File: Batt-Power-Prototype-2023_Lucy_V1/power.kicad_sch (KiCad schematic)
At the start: 62 parts, among them J1 Conn_01x02_Pin, U1 RPA60-2412SFW, U3 AZ1117IH-5.0, U5 AP62250Z6, U5 AZ1117-3.3

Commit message: added a bunch of footprints and other stuff...
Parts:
- CESH107M100AH4AA1: renamed from C1; footprint Capacitor_THT:CP_Radial_D8.0mm_P3.50mm -> Capacitor_THT:CP_Radial_D10.0mm_P5.00mm
- D2: footprint (none) -> Package_TO_SOT_SMD:TO-252-3_TabPin2
- renumbered C3 to needstobe2kv1, C4 to needstobe2kv2, C2 to needstobe50V1
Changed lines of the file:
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@@
   (junction (at 102.87 54.61) (diameter 0) (color 0 0 0 0)
   )
-  (junction (at 49.53 45.72) (diameter 0) (color 0 0 0 0)
-  )
   (junction (at 123.19 124.46) (diameter 0) (color 0 0 0 0)
   )
@@
   (junction (at 148.59 40.64) (diameter 0) (color 0 0 0 0)
   )
-  (junction (at 49.53 35.56) (diameter 0) (color 0 0 0 0)
-  )
   (junction (at 245.11 120.65) (diameter 0) (color 0 0 0 0)
   )
@@
     (stroke (width 0) (type default))
   )
-  (wire (pts (xy 49.53 35.56) (xy 49.53 36.83))
-    (stroke (width 0) (type default))
-  )
   (wire (pts (xy 134.62 105.41) (xy 134.62 124.46))
     (stroke (width 0) (type default))
@@
     (stroke (width 0) (type default))
   )
-  (wire (pts (xy 49.53 45.72) (xy 55.88 45.72))
+  (wire (pts (xy 33.02 45.72) (xy 55.88 45.72))
     (stroke (width 0) (type default))
   )
@@
     (stroke (width 0) (type default))
   )
-  (wire (pts (xy 49.53 35.56) (xy 55.88 35.56))
-    (stroke (width 0) (type default))
-  )
   (wire (pts (xy 105.41 93.98) (xy 99.06 93.98))
     (stroke (width 0) (type default))
@@
     (stroke (width 0) (type default))
   )
-  (wire (pts (xy 48.26 35.56) (xy 49.53 35.56))
+  (wire (pts (xy 48.26 35.56) (xy 55.88 35.56))
     (stroke (width 0) (type default))
   )
@@
     (stroke (width 0) (type default))
   )
-  (wire (pts (xy 49.53 45.72) (xy 49.53 44.45))
-    (stroke (width 0) (type default))
-  )
   (wire (pts (xy 180.34 29.21) (xy 180.34 30.48))
     (stroke (width 0) (type default))
@@
     (stroke (width 0) (type default))
   )
-  (wire (pts (xy 33.02 45.72) (xy 49.53 45.72))
-    (stroke (width 0) (type default))
-  )
   (wire (pts (xy 93.98 43.18) (xy 93.98 45.72))
     (stroke (width 0) (type default))
@@
   )
   (symbol (lib_id "Jumper:SolderJumper_2_Open") (at 102.87 59.69 90) (unit 1)
-    (in_bom yes) (on_board yes) (dnp no) (fields_autoplaced)
+    (in_bom yes) (on_board yes) (dnp no)
     (property "Reference" "JP2" (at 105.41 58.42 90)
       (effects (font (size 1.27 1.27)) (justify right))
     )
-    (property "Value" "SolderJumper_2_Open" (at 105.41 60.96 90)
+    (property "Value" "SolderJumper_2_Open" (at 104.14 63.5 90)
       (effects (font (size 1.27 1.27)) (justify right))
     )
@@
       (effects (font (size 1.27 1.27)) hide)
     )
-    (pin "2")
     (pin "1")
+    (pin "2")
     (instances
       (project "Batt-Power-Prototype-2023_Lucy_V1"
@@
   (symbol (lib_id "Device:C") (at 129.54 25.4 90) (unit 1)
     (in_bom yes) (on_board yes) (dnp no) (fields_autoplaced)
-    (property "Reference" "C3" (at 129.54 17.78 90)
-      (effects (font (size 1.27 1.27)))
+    (property "Reference" "needstobe2kv1" (at 129.54 17.78 90)
+      (effects (font (size 1.27 1.27)) hide)
     )
     (property "Value" "6.8n" (at 129.54 20.32 90)
@@
       (project "Batt-Power-Prototype-2023_Lucy_V1"
         (path "/c58627b7-5b67-4b57-b29b-cc34a75a9096/caf32978-5421-40df-803f-f9402117c79f"
-          (reference "C3") (unit 1)
+          (reference "needstobe2kv1") (unit 1)
         )
       )
@@
   (symbol (lib_id "Device:C") (at 102.87 40.64 0) (unit 1)
     (in_bom yes) (on_board yes) (dnp no)
-    (property "Reference" "C2" (at 97.79 39.37 0)
-      (effects (font (size 1.27 1.27)) (justify left))
+    (property "Reference" "needstobe50V1" (at 96.52 39.37 0)
+      (effects (font (size 1.27 1.27)) (justify left) hide)
     )
-    (property "Value" "10u" (at 97.79 41.91 0)
+    (property "Value" "10u" (at 96.52 40.64 0)
       (effects (font (size 1.27 1.27)) (justify left))
     )
@@
       (effects (font (size 1.27 1.27)) hide)
     )
-    (property "Datasheet" "~" (at 102.87 40.64 0)
+    (property "Datasheet" "" (at 102.87 40.64 0)
       (effects (font (size 1.27 1.27)) hide)
     )
@@
       (project "Batt-Power-Prototype-2023_Lucy_V1"
         (path "/c58627b7-5b67-4b57-b29b-cc34a75a9096/caf32978-5421-40df-803f-f9402117c79f"
-          (reference "C2") (unit 1)
+          (reference "needstobe50V1") (unit 1)
         )
       )
@@
   (symbol (lib_id "Device:C") (at 129.54 54.61 270) (unit 1)
     (in_bom yes) (on_board yes) (dnp no)
-    (property "Reference" "C4" (at 129.54 58.42 90)
-      (effects (font (size 1.27 1.27)))
+    (property "Reference" "needstobe2kv2" (at 129.54 58.42 90)
+      (effects (font (size 1.27 1.27)) hide)
     )
     (property "Value" "6.8n" (at 129.54 60.96 90)
@@
       (project "Batt-Power-Prototype-2023_Lucy_V1"
         (path "/c58627b7-5b67-4b57-b29b-cc34a75a9096/caf32978-5421-40df-803f-f9402117c79f"
-          (reference "C4") (unit 1)
+          (reference "needstobe2kv2") (unit 1)
         )
       )
@@
       (effects (font (size 1.27 1.27)))
     )
-    (property "Footprint" "" (at 68.58 35.56 0)
+    (property "Footprint" "Package_TO_SOT_SMD:TO-252-3_TabPin2" (at 68.58 35.56 0)
       (effects (font (size 1.27 1.27)) hide)
     )
@@
   (symbol (lib_id "Device:C_Polarized") (at 74.93 40.64 0) (unit 1)
     (in_bom yes) (on_board yes) (dnp no) (fields_autoplaced)
-    (property "Reference" "C1" (at 78.74 38.481 0)
-      (effects (font (size 1.27 1.27)) (justify left))
+    (property "Reference" "CESH107M100AH4AA1" (at 78.74 38.481 0)
+      (effects (font (size 1.27 1.27)) (justify left) hide)
     )
     (property "Value" "100u" (at 78.74 41.021 0)
       (effects (font (size 1.27 1.27)) (justify left))
     )
-    (property "Footprint" "Capacitor_THT:CP_Radial_D8.0mm_P3.50mm" (at 75.8952 44.45 0)
+    (property "Footprint" "Capacitor_THT:CP_Radial_D10.0mm_P5.00mm" (at 75.8952 44.45 0)
       (effects (font (size 1.27 1.27)) hide)
     )
-    (property "Datasheet" "~" (at 74.93 40.64 0)
+    (property "Datasheet" "https://connect.kemet.com:7667/gateway/IntelliData-ComponentDocumentation/1.0/download/datasheet/ESH107M100AH4AA" (at 74.93 40.64 0)
       (effects (font (size 1.27 1.27)) hide)
     )
@@
       (project "Batt-Power-Prototype-2023_Lucy_V1"
         (path "/c58627b7-5b67-4b57-b29b-cc34a75a9096/caf32978-5421-40df-803f-f9402117c79f"
-          (reference "C1") (unit 1)
+          (reference "CESH107M100AH4AA1") (unit 1)
         )
       )

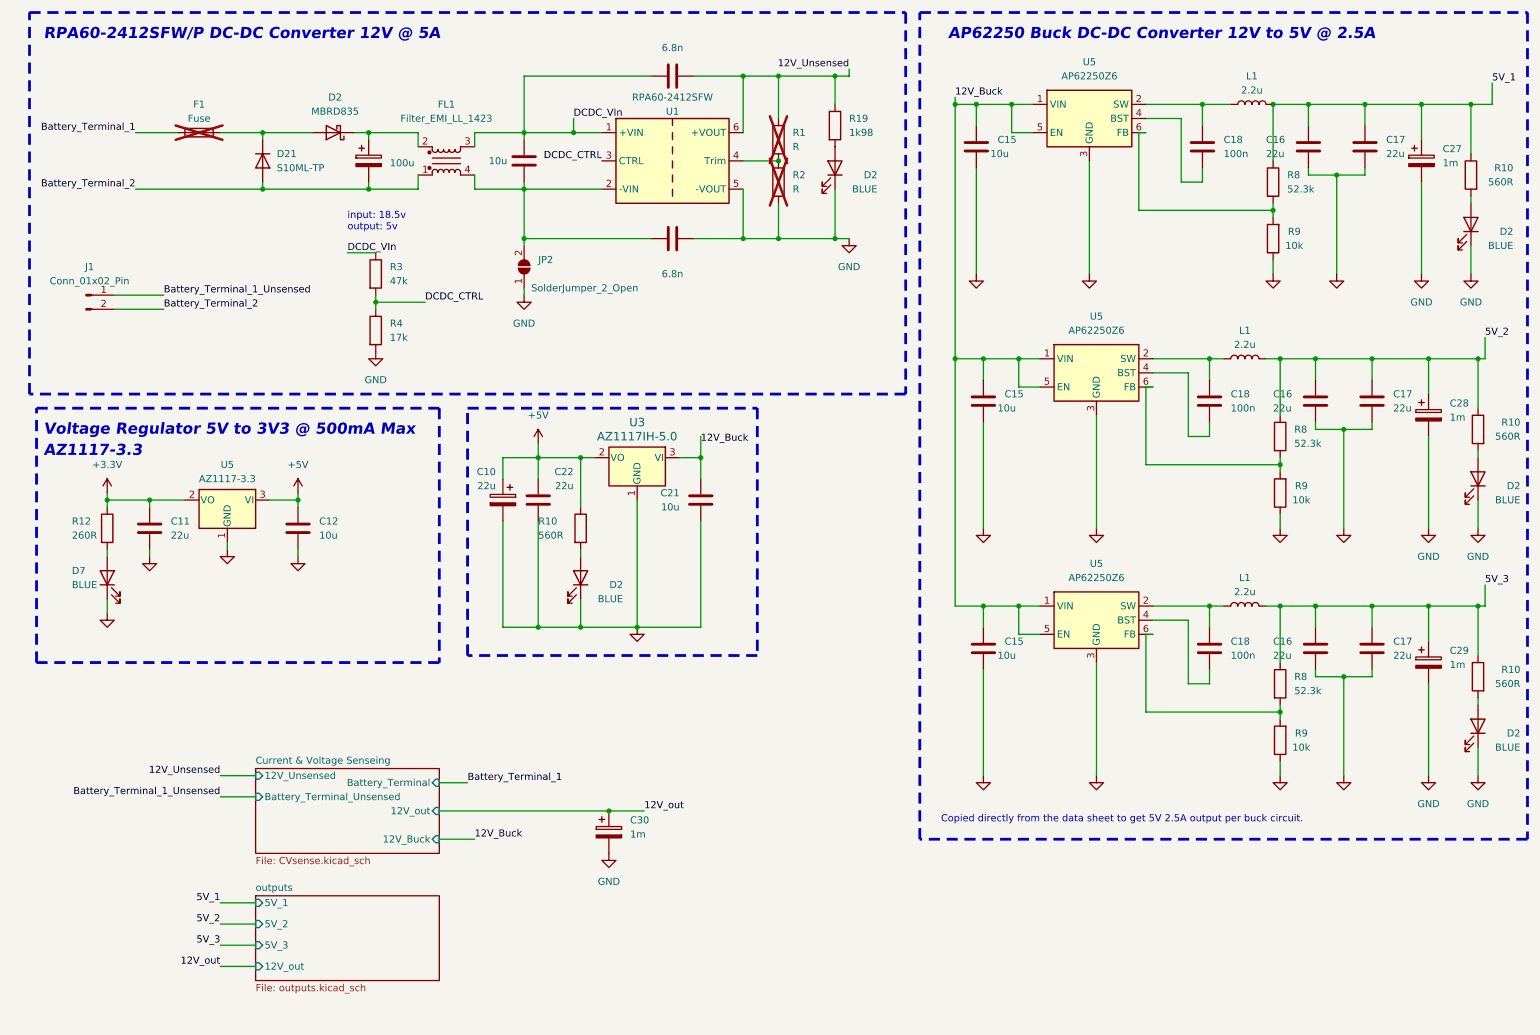
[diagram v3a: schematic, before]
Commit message: added a bunch of foot prints and 3d models
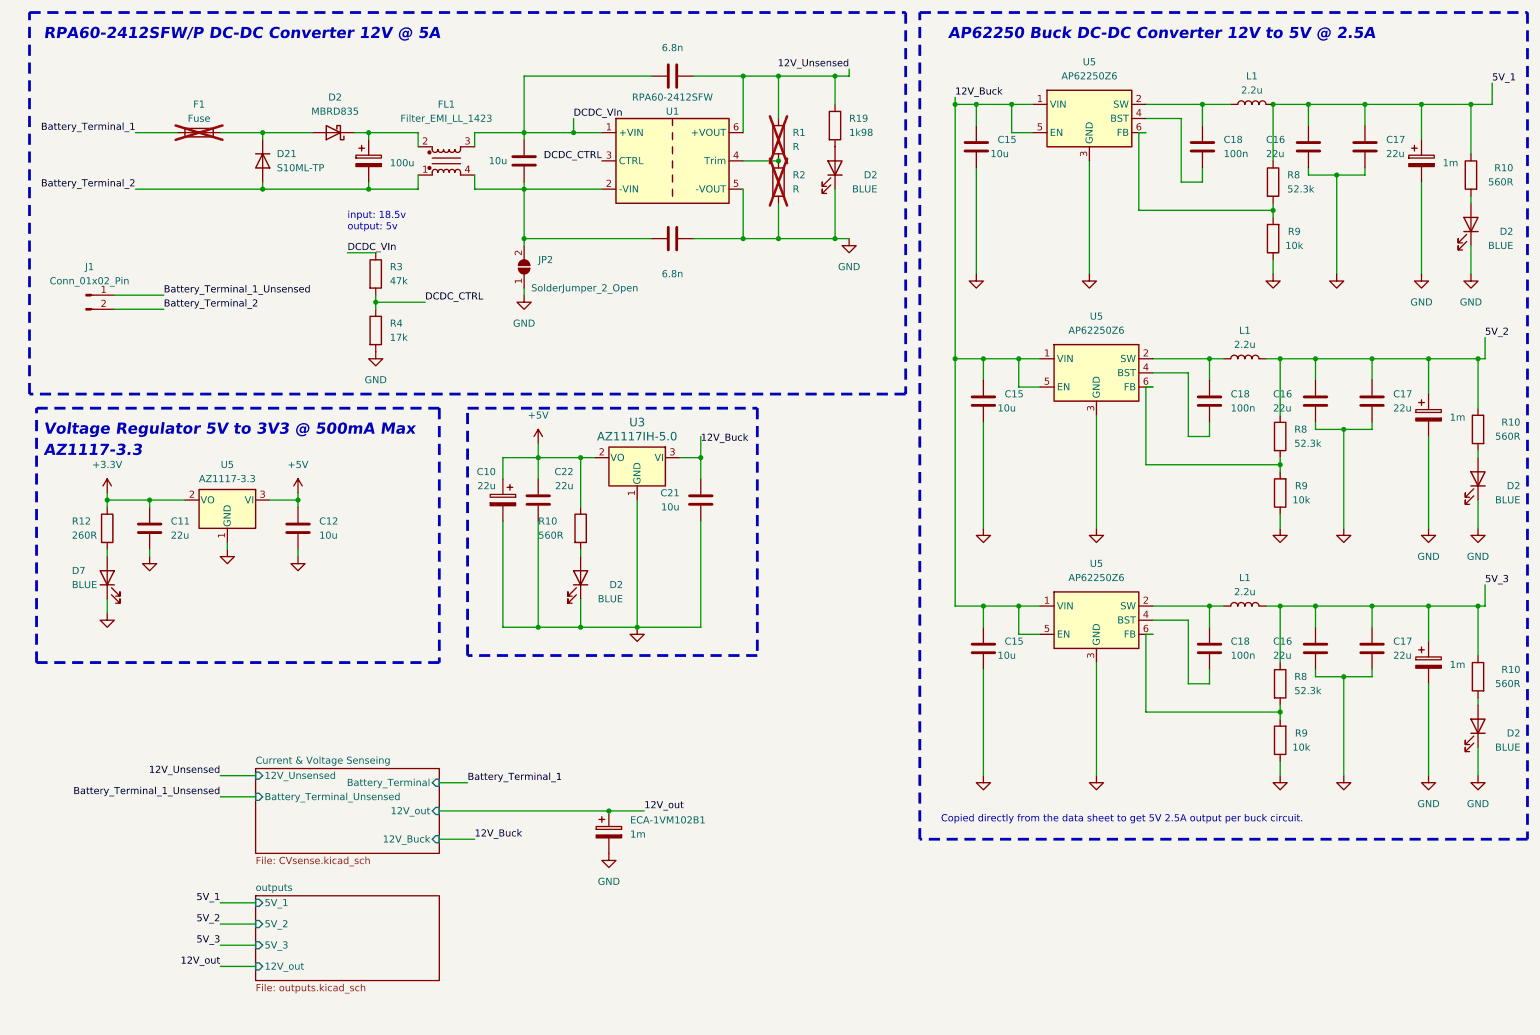
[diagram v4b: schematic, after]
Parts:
- ECA-1VM102B1: renamed from C30; footprint (none) -> Capacitor_THT:CP_Radial_D12.5mm_P5.00mm
- ECA-1VM102B2: renamed from C27; footprint Capacitor_SMD:CP_Elec_6.3x5.9 -> Capacitor_THT:CP_Radial_D12.5mm_P5.00mm
- ECA-1VM102B3: renamed from C28; footprint Capacitor_SMD:CP_Elec_6.3x5.9 -> Capacitor_THT:CP_Radial_D12.5mm_P5.00mm
- ECA-1VM102B4: renamed from C29; footprint Capacitor_SMD:CP_Elec_6.3x5.9 -> Capacitor_THT:CP_Radial_D12.5mm_P5.00mm
- JP2: footprint (none) -> Jumper:SolderJumper-2_P1.3mm_Open_RoundedPad1.0x1.5mm
- L1, R1, R19, R2, R3, R4, R8, R9: footprint (none) -> Resistor_SMD:R_0805_2012Metric
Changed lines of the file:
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@@
   (symbol (lib_id "Device:C_Polarized") (at 264.16 40.64 0) (unit 1)
     (in_bom yes) (on_board yes) (dnp no) (fields_autoplaced)
-    (property "Reference" "C27" (at 267.97 38.481 0)
-      (effects (font (size 1.27 1.27)) (justify left))
+    (property "Reference" "ECA-1VM102B2" (at 267.97 38.481 0)
+      (effects (font (size 1.27 1.27)) (justify left) hide)
     )
     (property "Value" "1m" (at 267.97 41.021 0)
       (effects (font (size 1.27 1.27)) (justify left))
     )
-    (property "Footprint" "Capacitor_SMD:CP_Elec_6.3x5.9" (at 265.1252 44.45 0)
+    (property "Footprint" "Capacitor_THT:CP_Radial_D12.5mm_P5.00mm" (at 265.1252 44.45 0)
       (effects (font (size 1.27 1.27)) hide)
     )
@@
       (project "Batt-Power-Prototype-2023_Lucy_V1"
         (path "/c58627b7-5b67-4b57-b29b-cc34a75a9096/caf32978-5421-40df-803f-f9402117c79f"
-          (reference "C27") (unit 1)
+          (reference "ECA-1VM102B2") (unit 1)
         )
       )
@@
       (effects (font (size 1.27 1.27)) (justify left))
     )
-    (property "Footprint" "" (at 74.422 60.96 90)
+    (property "Footprint" "Resistor_SMD:R_0805_2012Metric" (at 74.422 60.96 90)
       (effects (font (size 1.27 1.27)) hide)
     )
@@
   (symbol (lib_id "Device:C_Polarized") (at 265.43 86.36 0) (unit 1)
     (in_bom yes) (on_board yes) (dnp no) (fields_autoplaced)
-    (property "Reference" "C28" (at 269.24 84.201 0)
-      (effects (font (size 1.27 1.27)) (justify left))
+    (property "Reference" "ECA-1VM102B3" (at 269.24 84.201 0)
+      (effects (font (size 1.27 1.27)) (justify left) hide)
     )
     (property "Value" "1m" (at 269.24 86.741 0)
       (effects (font (size 1.27 1.27)) (justify left))
     )
-    (property "Footprint" "Capacitor_SMD:CP_Elec_6.3x5.9" (at 266.3952 90.17 0)
+    (property "Footprint" "Capacitor_THT:CP_Radial_D12.5mm_P5.00mm" (at 266.3952 90.17 0)
       (effects (font (size 1.27 1.27)) hide)
     )
@@
       (project "Batt-Power-Prototype-2023_Lucy_V1"
         (path "/c58627b7-5b67-4b57-b29b-cc34a75a9096/caf32978-5421-40df-803f-f9402117c79f"
-          (reference "C28") (unit 1)
+          (reference "ECA-1VM102B3") (unit 1)
         )
       )
@@
       (effects (font (size 1.27 1.27)))
     )
-    (property "Footprint" "" (at 240.538 144.78 90)
+    (property "Footprint" "Resistor_SMD:R_0805_2012Metric" (at 240.538 144.78 90)
       (effects (font (size 1.27 1.27)) hide)
     )
@@
       (effects (font (size 1.27 1.27)) (justify left))
     )
-    (property "Footprint" "" (at 235.712 44.45 90)
+    (property "Footprint" "Resistor_SMD:R_0805_2012Metric" (at 235.712 44.45 90)
       (effects (font (size 1.27 1.27)) hide)
     )
@@
       (effects (font (size 1.27 1.27)))
     )
-    (property "Footprint" "" (at 233.68 30.48 0)
+    (property "Footprint" "Resistor_SMD:R_0805_2012Metric" (at 233.68 30.48 0)
       (effects (font (size 1.27 1.27)) hide)
     )
@@
       (effects (font (size 1.27 1.27)) (justify right))
     )
-    (property "Footprint" "" (at 102.87 59.69 0)
+    (property "Footprint" "Jumper:SolderJumper-2_P1.3mm_Open_RoundedPad1.0x1.5mm" (at 102.87 59.69 0)
       (effects (font (size 1.27 1.27)) hide)
     )
@@
       (effects (font (size 1.27 1.27)))
     )
-    (property "Footprint" "" (at 232.41 76.2 0)
+    (property "Footprint" "Resistor_SMD:R_0805_2012Metric" (at 232.41 76.2 0)
       (effects (font (size 1.27 1.27)) hide)
     )
@@
   (symbol (lib_id "Device:C_Polarized") (at 265.43 130.81 0) (unit 1)
     (in_bom yes) (on_board yes) (dnp no) (fields_autoplaced)
-    (property "Reference" "C29" (at 269.24 128.651 0)
-      (effects (font (size 1.27 1.27)) (justify left))
+    (property "Reference" "ECA-1VM102B4" (at 269.24 128.651 0)
+      (effects (font (size 1.27 1.27)) (justify left) hide)
     )
     (property "Value" "1m" (at 269.24 131.191 0)
       (effects (font (size 1.27 1.27)) (justify left))
     )
-    (property "Footprint" "Capacitor_SMD:CP_Elec_6.3x5.9" (at 266.3952 134.62 0)
+    (property "Footprint" "Capacitor_THT:CP_Radial_D12.5mm_P5.00mm" (at 266.3952 134.62 0)
       (effects (font (size 1.27 1.27)) hide)
     )
@@
       (project "Batt-Power-Prototype-2023_Lucy_V1"
         (path "/c58627b7-5b67-4b57-b29b-cc34a75a9096/caf32978-5421-40df-803f-f9402117c79f"
-          (reference "C29") (unit 1)
+          (reference "ECA-1VM102B4") (unit 1)
         )
       )
@@
       (effects (font (size 1.27 1.27)) (justify left))
     )
-    (property "Footprint" "" (at 236.982 134.62 90)
+    (property "Footprint" "Resistor_SMD:R_0805_2012Metric" (at 236.982 134.62 90)
       (effects (font (size 1.27 1.27)) hide)
     )
@@
       (effects (font (size 1.27 1.27)))
     )
-    (property "Footprint" "" (at 232.41 120.65 0)
+    (property "Footprint" "Resistor_SMD:R_0805_2012Metric" (at 232.41 120.65 0)
       (effects (font (size 1.27 1.27)) hide)
     )
@@
       (effects (font (size 1.27 1.27)))
     )
-    (property "Footprint" "" (at 240.538 100.33 90)
+    (property "Footprint" "Resistor_SMD:R_0805_2012Metric" (at 240.538 100.33 90)
       (effects (font (size 1.27 1.27)) hide)
     )
@@
       (effects (font (size 1.27 1.27)) (justify left))
     )
-    (property "Footprint" "" (at 146.812 36.83 90)
+    (property "Footprint" "Resistor_SMD:R_0805_2012Metric" (at 146.812 36.83 90)
       (effects (font (size 1.27 1.27)) hide)
     )
@@
       (effects (font (size 1.27 1.27)) (justify left))
     )
-    (property "Footprint" "" (at 146.812 44.45 90)
+    (property "Footprint" "Resistor_SMD:R_0805_2012Metric" (at 146.812 44.45 90)
       (effects (font (size 1.27 1.27)) hide)
     )
@@
       (effects (font (size 1.27 1.27)) (justify left))
     )
-    (property "Footprint" "" (at 236.982 90.17 90)
+    (property "Footprint" "Resistor_SMD:R_0805_2012Metric" (at 236.982 90.17 90)
       (effects (font (size 1.27 1.27)) hide)
     )
@@
   (symbol (lib_id "Device:C_Polarized") (at 118.11 161.29 0) (unit 1)
     (in_bom yes) (on_board yes) (dnp no) (fields_autoplaced)
-    (property "Reference" "C30" (at 121.92 159.131 0)
+    (property "Reference" "ECA-1VM102B1" (at 121.92 159.131 0)
       (effects (font (size 1.27 1.27)) (justify left))
     )
@@
       (effects (font (size 1.27 1.27)) (justify left))
     )
-    (property "Footprint" "" (at 119.0752 165.1 0)
+    (property "Footprint" "Capacitor_THT:CP_Radial_D12.5mm_P5.00mm" (at 119.0752 165.1 0)
       (effects (font (size 1.27 1.27)) hide)
     )
@@
       (project "Batt-Power-Prototype-2023_Lucy_V1"
         (path "/c58627b7-5b67-4b57-b29b-cc34a75a9096/caf32978-5421-40df-803f-f9402117c79f"
-          (reference "C30") (unit 1)
+          (reference "ECA-1VM102B1") (unit 1)
         )
       )
@@
       (effects (font (size 1.27 1.27)) (justify left))
     )
-    (property "Footprint" "" (at 74.422 71.12 90)
+    (property "Footprint" "Resistor_SMD:R_0805_2012Metric" (at 74.422 71.12 90)
       (effects (font (size 1.27 1.27)) hide)
     )
@@
       (effects (font (size 1.27 1.27)))
     )
-    (property "Footprint" "" (at 239.268 54.61 90)
+    (property "Footprint" "Resistor_SMD:R_0805_2012Metric" (at 239.268 54.61 90)
       (effects (font (size 1.27 1.27)) hide)
     )
@@
       (effects (font (size 1.27 1.27)) (justify left))
     )
-    (property "Footprint" "" (at 156.972 34.29 90)
-      (effects (font (size 1.27 1.27)) hide)
-    )
+    (property "Footprint" "Resistor_SMD:R_0805_2012Metric" (at 156.972 34.29 90)
+      (effects (font (size 1.27 1.27)) hide)
+    )

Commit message: i think schematic is done??
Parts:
- F1: value Fuse -> 3544-2; footprint (none) -> BP_FTP:CONN_3544-2_KEY
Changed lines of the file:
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@@
       (effects (font (size 1.27 1.27)))
     )
-    (property "Value" "Fuse" (at 44.45 33.02 90)
+    (property "Value" "3544-2" (at 44.45 33.02 90)
       (effects (font (size 1.27 1.27)))
     )
-    (property "Footprint" "" (at 44.45 37.338 90)
+    (property "Footprint" "BP_FTP:CONN_3544-2_KEY" (at 44.45 37.338 90)
       (effects (font (size 1.27 1.27)) hide)
     )

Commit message: made changes to schematic
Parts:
- removed C10: 22u, Capacitor_SMD:CP_Elec_6.3x5.9, symbol Device:C_Polarized
- removed D2: MBRD835, Package_TO_SOT_SMD:TO-252-3_TabPin2, symbol Device:D_Schottky
- added D22: MBRD835, Package_TO_SOT_SMD:TO-252-2, symbol Device:D_Schottky_KAA
- C?: renamed from ECA-1VM102B4; DigiKey (none) -> ECA-1VM102B4
- F1: now fitted
- renumbered needstobe2kv2 to C31
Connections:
- net 12V_Unsensed: now also ECA-1VM102B1.1
- net 12V_out: no longer ECA-1VM102B1.1
- net at CESH107M100AH4AA1.1, FL1.2: now also D22.2 (K)
- net at D21.1 (K), F1.2: now also D22.1 (A), D22.3 (A)
- net +3.3V renamed +3V3
- net DCDC_VIn renamed DCDC_V_{in}
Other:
- sheet Current & Voltage Senseing ports: added BAttery_Crrnt; removed none
- note added: "Needs to be 2.2kV"
- note added: "this part"
- moved on the sheet: C11, C12, C21, C22, D2, D7, ECA-1VM102B1, L1, R1, R12, R19, R2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
